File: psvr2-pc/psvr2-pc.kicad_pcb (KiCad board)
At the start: 2 copper layers, 127 x 61 mm, 18 parts, among them J2 USB3_B_Micro, J3 DP_47272, J4 USB_C_Receptacle_USB2.0_14P, P1 USB_C_Plug, Q1 IRLML6244, U1 RP2040, U2 M95256-WMN6P, U3 FUSB302B01MPX, U4 FUSB302B01MPX, Y1 Crystal

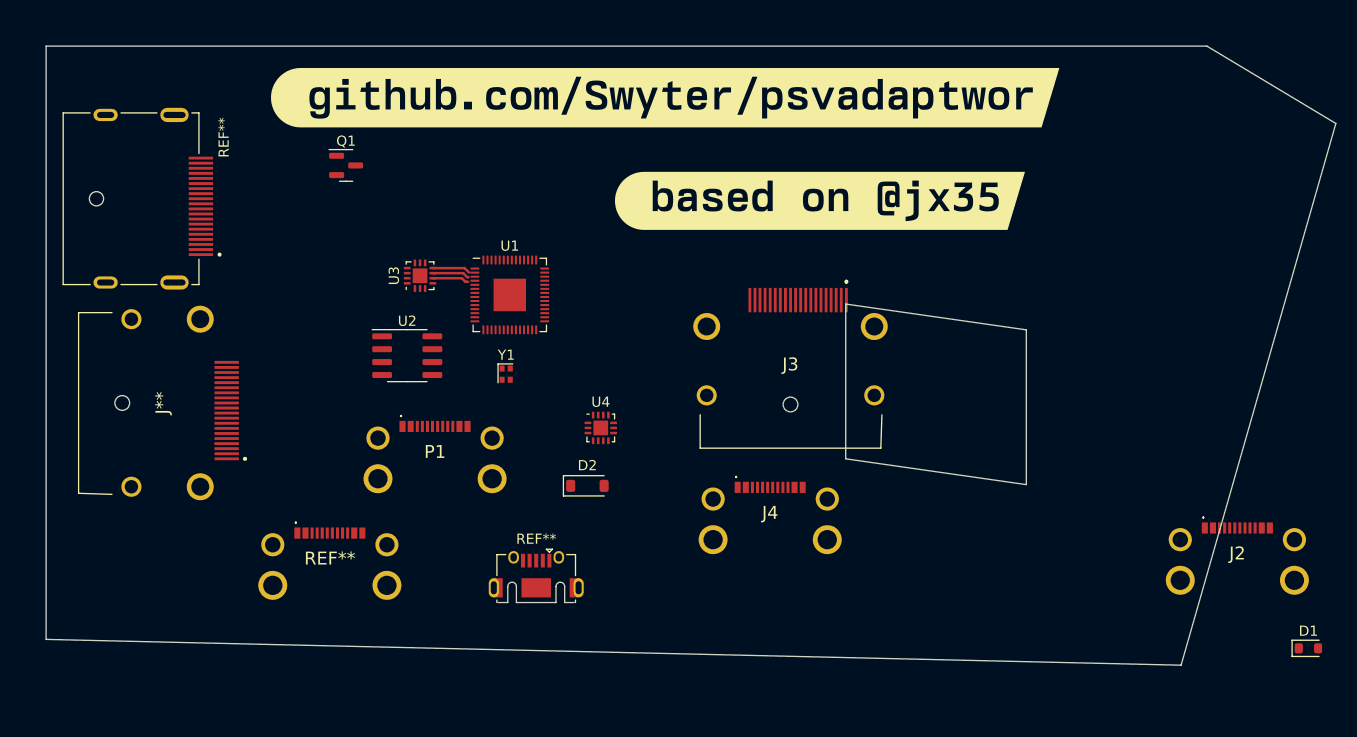
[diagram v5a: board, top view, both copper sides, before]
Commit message: Start cleaning things up the mess now that I know how to download and install actual footprints.
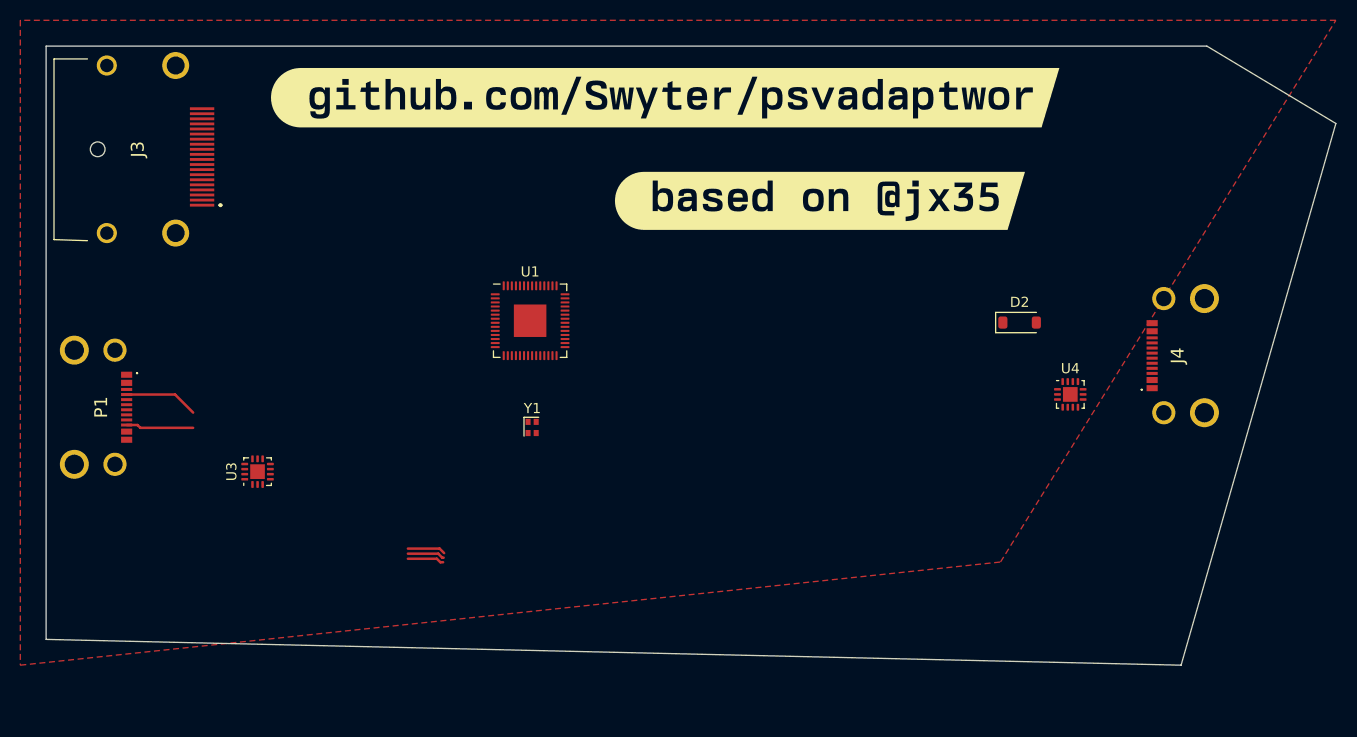
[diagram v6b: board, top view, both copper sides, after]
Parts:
- removed D1: BAT54GWJ, Diode_SMD:D_SOD-110
- removed J**: 472720001, Samacsys:472720001
- removed J2: USB3_B_Micro, Samacsys:2169900002
- removed Q1: IRLML6244, Package_TO_SOT_SMD:SOT-23
- removed REF**: 2169900002, Samacsys:2169900002
- removed REF**: USB_Micro-AB_Molex_47590-0001, Connector_USB:USB_Micro-AB_Molex_47590-0001
- removed REF**: MOLEX_47272-0001, Snapeda:47272-0001_MOLEX_47272-0001
- removed U2: M95256-WMN6P, Package_SO:SOIC-8_3.9x4.9mm_P1.27mm
- moved J3 68.9 mm to (20.8, 22.9), turned to -90 degrees
- moved U4 46.4 mm to (113.5, 47.0)
- moved D2 45.5 mm to (108.6, 39.9)
- moved J4 43.4 mm to (124.5, 43.2), turned to 90 degrees
- moved P1 33.6 mm to (17.8, 48.3), turned to -90 degrees
- moved U3 25.1 mm to (33.5, 54.6)
- moved Y1 5.84 mm to (60.6, 50.2)
- moved U1 3.23 mm to (60.4, 39.7)
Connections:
- D2 pad 1: Net-(D2-K) -> /HMD_VBUS
- J4 pad A5: Net-(J4-CC1) -> unconnected-(J4-CC1-PadA5)
- J4 pad B5: Net-(J4-CC2) -> unconnected-(J4-CC2-PadB5)
- P1 pad A4: Net-(U3-VBUS) -> /HMD_VBUS
- P1 pad A9: Net-(U3-VBUS) -> /HMD_VBUS
- P1 pad B4: Net-(U3-VBUS) -> /HMD_VBUS
- P1 pad B9: Net-(U3-VBUS) -> /HMD_VBUS
- U3 pad 15: Net-(U3-GND-Pad15) -> GND
- U3 pad 2: Net-(U3-VBUS) -> /HMD_VBUS
- U3 pad 3: Net-(U3-VDD-Pad3) -> +3.3V
- U3 pad 4: Net-(U3-VDD-Pad3) -> +3.3V
- U3 pad 8: Net-(U3-GND-Pad15) -> GND
- U3 pad 9: Net-(U3-GND-Pad15) -> GND
- U4 pad 1: Net-(J4-CC2) -> Net-(U4-CC2-Pad1)
- U4 pad 10: Net-(J4-CC1) -> Net-(U4-CC1-Pad10)
- U4 pad 11: Net-(J4-CC1) -> Net-(U4-CC1-Pad10)
- U4 pad 14: Net-(J4-CC2) -> Net-(U4-CC2-Pad1)
- U4 pad 15: Net-(U4-GND-Pad15) -> GND
- U4 pad 2: Net-(D2-K) -> unconnected-(U4-VBUS-Pad2)
- U4 pad 3: Net-(U4-VDD-Pad3) -> +3.3V
- U4 pad 4: Net-(U4-VDD-Pad3) -> +3.3V
- U4 pad 5: unconnected-(U4-INT_N-Pad5) -> /PWR_TYC_INT
- U4 pad 6: unconnected-(U4-SCL-Pad6) -> /PWR_TYC_SCL
- U4 pad 7: unconnected-(U4-SDA-Pad7) -> /PWR_TYC_SDA
- U4 pad 8: Net-(U4-GND-Pad15) -> GND
- U4 pad 9: Net-(U4-GND-Pad15) -> GND
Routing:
- net Net-(P1-CC): track 0.00 -> 7.28 mm
- net Net-(P1-VCONN): track 0.00 -> 6.66 mm
- added copper zone on F.Cu, net GND
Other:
- outline, holes or cut-outs redrawn

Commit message: Fix the micro USB footprint, rearrange the PCB now that more pieces appear. Add funkier labels.
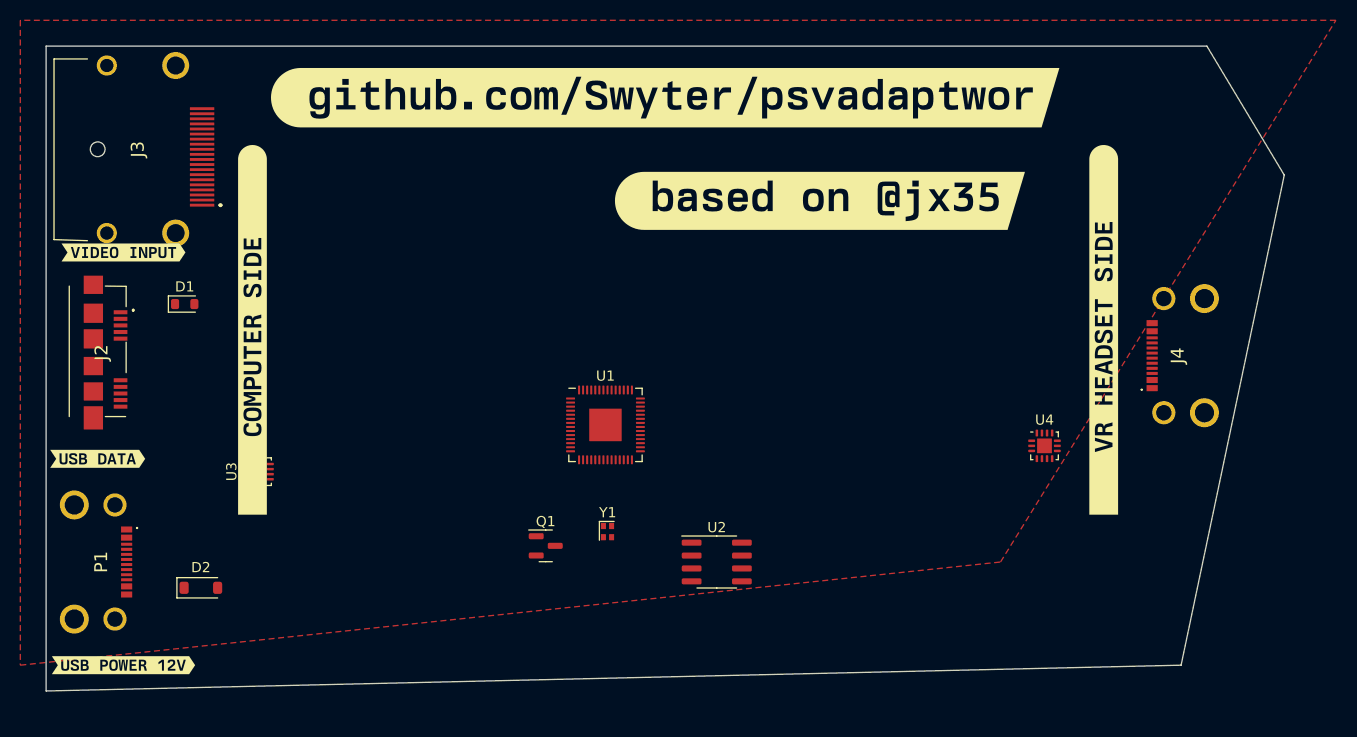
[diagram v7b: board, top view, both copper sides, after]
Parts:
- added D1: BAT54GWJ, Diode_SMD:D_SOD-110, F.Cu at (26.4, 38.1)
- added J2: USB3_B_Micro, Samacsys:692622030100, F.Cu at (17.8, 42.8)
- added Q1: IRLML6244, Package_TO_SOT_SMD:SOT-23, F.Cu at (61.9, 61.9)
- added U2: M95256-WMN6P, Package_SO:SOIC-8_3.9x4.9mm_P1.27mm, F.Cu at (78.7, 63.5)
- added kibuzzard-65C06FC7: G***, kibuzzard-65C06FC7, F.Cu at (116.8, 40.6)
- added kibuzzard-65C06FDA: G***, kibuzzard-65C06FDA, F.Cu at (33.0, 40.6)
- added kibuzzard-65C07004: G***, kibuzzard-65C07004, F.Cu at (20.3, 33.0)
- added kibuzzard-65C0700D: G***, kibuzzard-65C0700D, F.Cu at (17.8, 53.3)
- added kibuzzard-65C07017: G***, kibuzzard-65C07017, F.Cu at (20.3, 73.7)
- moved D2 84.7 mm to (27.9, 66.0)
- moved P1 15.2 mm to (17.8, 63.5)
- moved U1 12.7 mm to (67.8, 50.0)
- moved Y1 12.7 mm to (68.0, 60.5)
- moved U4 5.67 mm to (111.0, 52.1)
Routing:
- net Net-(P1-CC): track 7.28 -> 0.00 mm
- net Net-(P1-VCONN): track 6.66 -> 0.00 mm
- net /HMD_TYC_SDA: track 3.75 -> 0.00 mm
- net /HMD_TYC_SCL: track 3.68 -> 0.00 mm
- net /HMD_TYC_INT: track 3.61 -> 0.00 mm
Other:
- board size 127 x 61 mm -> 121.9 x 63.5 mm

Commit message: Add important stuff like changing the solder mask color to dark blue.
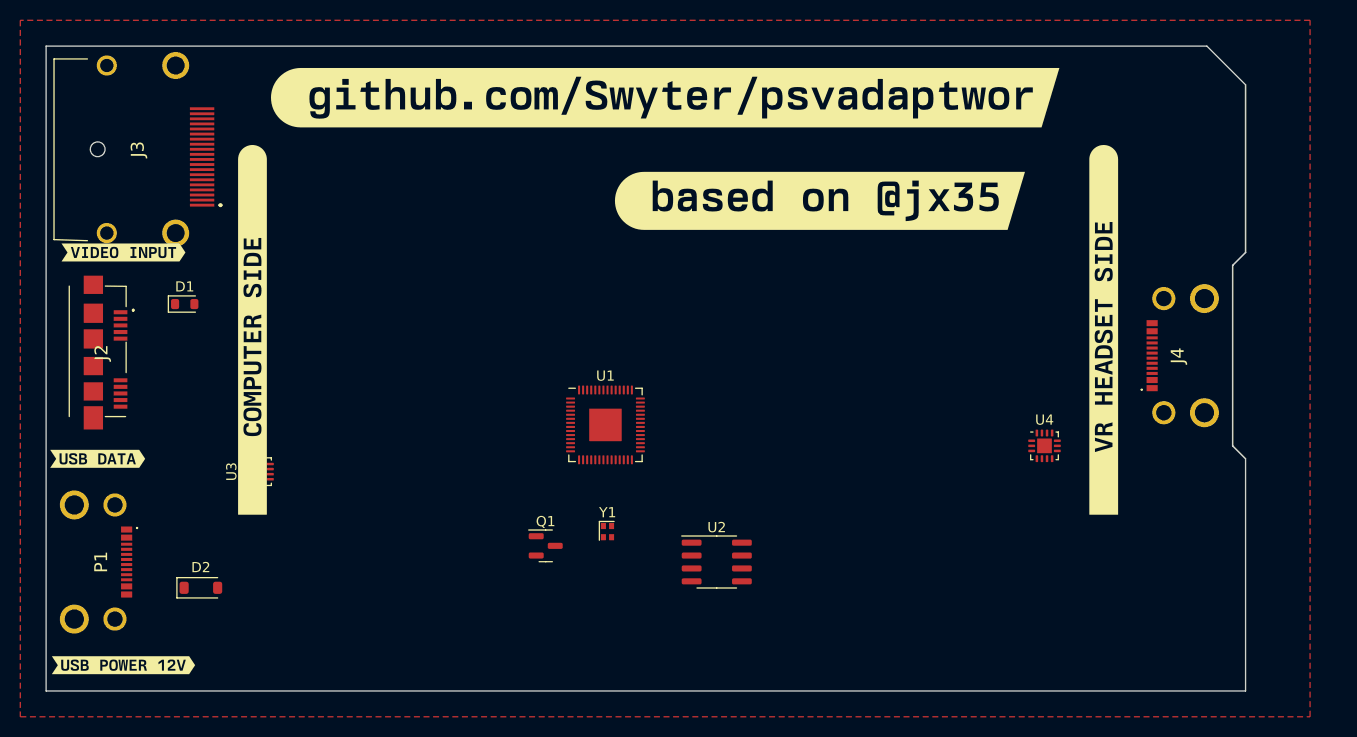
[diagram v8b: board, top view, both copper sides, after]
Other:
- board size 121.9 x 63.5 mm -> 118.1 x 63.5 mm
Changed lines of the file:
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@@
       (layer "F.SilkS" (type "Top Silk Screen"))
       (layer "F.Paste" (type "Top Solder Paste"))
-      (layer "F.Mask" (type "Top Solder Mask") (thickness 0.01))
+      (layer "F.Mask" (type "Top Solder Mask") (color "#2C5B80D4") (thickness 0.01))
       (layer "F.Cu" (type "copper") (thickness 0.035))
       (layer "dielectric 1" (type "core") (thickness 1.51) (material "FR4") (epsilon_r 4.5) (loss_tangent 0.02))
       (layer "B.Cu" (type "copper") (thickness 0.035))
-      (layer "B.Mask" (type "Bottom Solder Mask") (thickness 0.01))
+      (layer "B.Mask" (type "Bottom Solder Mask") (color "#2C5B80D4") (thickness 0.01))
       (layer "B.Paste" (type "Bottom Solder Paste"))
       (layer "B.SilkS" (type "Bottom Silk Screen"))
@@
       (stroke (width 0) (type solid)) (fill solid) (layer "F.SilkS"))
   )
-  (gr_line (start 134.62 25.4) (end 127 12.7)
+  (gr_line (start 129.54 52.07) (end 130.81 53.34)
+    (stroke (width 0.15) (type default)) (layer "Edge.Cuts"))
+  (gr_line (start 130.81 16.51) (end 127 12.7)
     (stroke (width 0.1) (type default)) (layer "Edge.Cuts"))
-  (gr_line (start 124.46 73.66) (end 134.62 25.4)
+  (gr_line (start 130.81 76.2) (end 130.81 53.34)
     (stroke (width 0.1) (type default)) (layer "Edge.Cuts"))
+  (gr_line (start 130.81 16.51) (end 130.81 33.02)
+    (stroke (width 0.15) (type default)) (layer "Edge.Cuts"))
+  (gr_line (start 129.54 52.07) (end 129.54 34.29)
+    (stroke (width 0.15) (type default)) (layer "Edge.Cuts"))
   (gr_line (start 12.7 12.7) (end 12.7 76.2)
     (stroke (width 0.1) (type default)) (layer "Edge.Cuts"))
   (gr_line (start 127 12.7) (end 12.7 12.7)
     (stroke (width 0.1) (type default)) (layer "Edge.Cuts"))
-  (gr_line (start 12.7 76.2) (end 124.46 73.66)
+  (gr_line (start 12.7 76.2) (end 130.81 76.2)
     (stroke (width 0.1) (type default)) (layer "Edge.Cuts"))
+  (gr_line (start 130.81 76.2) (end 130.81 76.2)
+    (stroke (width 0.1) (type default)) (layer "Edge.Cuts"))
+  (gr_line (start 130.81 76.2) (end 130.81 76.2)
+    (stroke (width 0.1) (type default)) (layer "Edge.Cuts"))
+  (gr_line (start 129.54 34.29) (end 130.81 33.02)
+    (stroke (width 0.15) (type default)) (layer "Edge.Cuts"))
   (zone (net 51) (net_name "GND") (layer "F.Cu") (hatch edge 0.5)
     (connect_pads (clearance 0.5))
@@
       (pts
         (xy 10.16 10.16)
-        (xy 10.16 73.66)
-        (xy 106.68 63.5)
-        (xy 139.7 10.16)
+        (xy 10.16 78.74)
+        (xy 137.16 78.74)
+        (xy 137.16 10.16)
       )
     )
